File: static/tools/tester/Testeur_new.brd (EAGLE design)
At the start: 103.5 x 105.7 mm, 28 parts, among them IC1 MEGA8-P, SW1 CI-11

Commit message: [tester] add VCC pin for UART
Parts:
- removed UART: (no value), con-lstb:MA03-1
- added SV1: (no value), con-lstb:MA04-1
- moved R1 6.38 mm to (15.9, 9.53)
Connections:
- net GND: now also SV1.3; no longer UART.3
- net N$21: now also SV1.1; no longer UART.1
- net N$22: now also SV1.2; no longer UART.2
- net VCC: now also SV1.4
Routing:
- net N$4: track 5.39 -> 11.5 mm
- net VCC: track 162.1 -> 163.9 mm
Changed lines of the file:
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@@
 <?xml version="1.0" encoding="utf-8"?>
 <!DOCTYPE eagle SYSTEM "eagle.dtd">
-<eagle version="6.1">
+<eagle version="6.3">
 <drawing>
 <settings>
@@
 </class>
 </classes>
-<designrules>
+<designrules name="default">
 <description language="de">&lt;b&gt;EAGLE Design Rules&lt;/b&gt;
 &lt;p&gt;
@@
 <element name="C1-REGULATOR" library="capacitor-wima" package="C5B5" value="" x="31.75" y="41.275" rot="R270"/>
 <element name="C2-REGULATOR" library="capacitor-wima" package="C5B5" value="" x="46.99" y="41.275" rot="R270"/>
-<element name="R1" library="rcl" package="0204/5" value="" x="15.24" y="15.875" rot="R90"/>
+<element name="R1" library="rcl" package="0204/5" value="" x="15.875" y="9.525" rot="R90"/>
 <element name="RETURN" library="con-lstb" package="MA03-1" value="" x="10.16" y="31.115" rot="R180">
 <attribute name="OC_NEWARK" value="unknown" x="-33.02" y="81.915" size="1.778" layer="27" rot="R180" display="off"/>
@@
 <attribute name="MF" value="" x="-11.43" y="-47.625" size="1.778" layer="27" rot="R270" display="off"/>
 <attribute name="OC_FARNELL" value="unknown" x="-11.43" y="-47.625" size="1.778" layer="27" rot="R270" display="off"/>
-</element>
-<element name="UART" library="con-lstb" package="MA03-1" value="" x="19.05" y="12.065" rot="R270">
-<attribute name="OC_NEWARK" value="unknown" x="-38.1" y="-5.715" size="1.778" layer="27" rot="R270" display="off"/>
-<attribute name="MPN" value="" x="-38.1" y="-5.715" size="1.778" layer="27" rot="R270" display="off"/>
-<attribute name="MF" value="" x="-38.1" y="-5.715" size="1.778" layer="27" rot="R270" display="off"/>
-<attribute name="OC_FARNELL" value="unknown" x="-38.1" y="-5.715" size="1.778" layer="27" rot="R270" display="off"/>
 </element>
 <element name="I²C" library="con-lstb" package="MA04-1" value="" x="8.89" y="23.495">
@@
 <attribute name="MF" value="" x="93.98" y="12.7" size="1.778" layer="27" display="off"/>
 <attribute name="OC_FARNELL" value="unknown" x="93.98" y="12.7" size="1.778" layer="27" display="off"/>
+</element>
+<element name="SV1" library="con-lstb" package="MA04-1" value="" x="19.05" y="10.795" rot="R270">
+<attribute name="OC_NEWARK" value="unknown" x="19.05" y="10.795" size="1.778" layer="27" rot="R270" display="off"/>
+<attribute name="MPN" value="" x="19.05" y="10.795" size="1.778" layer="27" rot="R270" display="off"/>
+<attribute name="MF" value="" x="19.05" y="10.795" size="1.778" layer="27" rot="R270" display="off"/>
+<attribute name="OC_FARNELL" value="unknown" x="19.05" y="10.795" size="1.778" layer="27" rot="R270" display="off"/>
 </element>
 </elements>
@@
 <contactref element="IC1" pad="1"/>
 <contactref element="R1" pad="2"/>
-<wire x1="15.24" y1="18.415" x2="19.05" y2="22.225" width="0.8128" layer="16"/>
+<wire x1="15.875" y1="12.065" x2="15.875" y2="19.05" width="0.8128" layer="16"/>
+<wire x1="15.875" y1="19.05" x2="19.05" y2="22.225" width="0.8128" layer="16"/>
 </signal>
 <signal name="N$7">
@@
 <wire x1="41.91" y1="36.83" x2="39.37" y2="34.29" width="0.8128" layer="16"/>
 <wire x1="39.37" y1="34.29" x2="39.37" y2="29.845" width="0.8128" layer="16"/>
-<wire x1="15.24" y1="13.335" x2="10.16" y2="13.335" width="0.8128" layer="16"/>
 <wire x1="10.16" y1="13.335" x2="8.89" y2="14.605" width="0.8128" layer="16"/>
 <wire x1="8.89" y1="14.605" x2="8.89" y2="15.875" width="0.8128" layer="16"/>
@@
 <via x="34.29" y="19.05" extent="1-16" drill="0.8"/>
 <via x="31.75" y="7.62" extent="1-16" drill="0.8"/>
-<wire x1="26.67" y1="9.525" x2="24.13" y2="9.525" width="0.8128" layer="16"/>
-<wire x1="24.13" y1="9.525" x2="22.86" y2="10.795" width="0.8128" layer="16"/>
 <wire x1="29.845" y1="7.62" x2="27.94" y2="9.525" width="0.8128" layer="16"/>
 <wire x1="27.94" y1="9.525" x2="26.67" y2="9.525" width="0.8128" layer="16"/>
-<wire x1="15.24" y1="13.335" x2="15.24" y2="11.43" width="0.8128" layer="16"/>
-<wire x1="15.24" y1="11.43" x2="15.24" y2="9.525" width="0.8128" layer="1"/>
-<wire x1="15.24" y1="9.525" x2="17.145" y2="7.62" width="0.8128" layer="1"/>
-<wire x1="17.145" y1="7.62" x2="20.955" y2="7.62" width="0.8128" layer="1"/>
-<wire x1="20.955" y1="7.62" x2="22.86" y2="9.525" width="0.8128" layer="1"/>
-<wire x1="22.86" y1="9.525" x2="22.86" y2="10.795" width="0.8128" layer="1"/>
-<via x="15.24" y="11.43" extent="1-16" drill="0.8"/>
+<wire x1="15.875" y1="6.985" x2="15.875" y2="4.445" width="0.8128" layer="16"/>
+<wire x1="15.875" y1="4.445" x2="20.955" y2="4.445" width="0.8128" layer="1"/>
+<wire x1="20.955" y1="4.445" x2="22.86" y2="6.35" width="0.8128" layer="1"/>
+<wire x1="22.86" y1="6.35" x2="22.86" y2="10.795" width="0.8128" layer="1"/>
+<via x="15.875" y="4.445" extent="1-16" drill="0.8"/>
 <via x="22.86" y="10.795" extent="1-16" drill="0.8"/>
 <wire x1="12.7" y1="6.985" x2="7.62" y2="6.985" width="0.8128" layer="16"/>
@@
 <wire x1="3.81" y1="17.78" x2="5.08" y2="19.05" width="0.8128" layer="16"/>
 <wire x1="5.08" y1="19.05" x2="5.08" y2="20.32" width="0.8128" layer="16"/>
+<contactref element="SV1" pad="4"/>
+<wire x1="12.7" y1="6.985" x2="15.875" y2="6.985" width="0.8128" layer="16"/>
+<wire x1="19.05" y1="6.985" x2="15.875" y2="6.985" width="0.8128" layer="16"/>
+<wire x1="24.13" y1="9.525" x2="22.86" y2="10.795" width="0.8128" layer="16"/>
+<wire x1="26.67" y1="9.525" x2="24.13" y2="9.525" width="0.8128" layer="16"/>
 </signal>
 <signal name="GND">
@@
 <contactref element="POTAR-CONTRASTE" pad="3"/>
 <contactref element="CODER-MOTOR" pad="4"/>
-<contactref element="UART" pad="3"/>
 <contactref element="I²C" pad="2"/>
 <contactref element="IC1" pad="22"/>
@@
 <wire x1="7.62" y1="41.91" x2="7.62" y2="36.83" width="0.8128" layer="16"/>
 <wire x1="7.62" y1="36.83" x2="7.62" y2="31.115" width="0.8128" layer="16"/>
-<wire x1="19.05" y1="9.525" x2="19.685" y2="9.525" width="0.8128" layer="16"/>
-<wire x1="19.685" y1="9.525" x2="22.225" y2="6.985" width="0.8128" layer="16"/>
 <wire x1="22.225" y1="6.985" x2="26.67" y2="6.985" width="0.8128" layer="16"/>
 <wire x1="26.67" y1="6.985" x2="27.305" y2="6.985" width="0.8128" layer="16"/>
@@
 <wire x1="12.065" y1="43.815" x2="9.525" y2="43.815" width="0.8128" layer="16"/>
 <wire x1="9.525" y1="43.815" x2="7.62" y2="41.91" width="0.8128" layer="16"/>
-<wire x1="19.05" y1="9.525" x2="12.7" y2="9.525" width="0.8128" layer="16"/>
 <wire x1="12.7" y1="9.525" x2="7.62" y2="9.525" width="0.8128" layer="16"/>
 <wire x1="6.35" y1="15.875" x2="6.35" y2="13.97" width="0.8128" layer="16"/>
@@
 <wire x1="19.05" y1="41.275" x2="19.05" y2="42.545" width="0.8128" layer="16"/>
 <wire x1="34.29" y1="36.195" x2="31.75" y2="38.735" width="0.8128" layer="16"/>
+<contactref element="SV1" pad="3"/>
+<wire x1="12.7" y1="9.525" x2="19.05" y2="9.525" width="0.8128" layer="16"/>
+<wire x1="22.225" y1="6.985" x2="19.685" y2="9.525" width="0.8128" layer="16"/>
+<wire x1="19.685" y1="9.525" x2="19.05" y2="9.525" width="0.8128" layer="16"/>
 </signal>
 <signal name="N$14">
@@
 <signal name="N$21">
 <contactref element="IC1" pad="2"/>
-<contactref element="UART" pad="1"/>
-<wire x1="19.05" y1="14.605" x2="21.59" y2="17.145" width="0.8128" layer="16"/>
-<wire x1="21.59" y1="17.145" x2="21.59" y2="22.225" width="0.8128" layer="16"/>
+<wire x1="21.59" y1="16.51" x2="21.59" y2="22.225" width="0.8128" layer="16"/>
+<contactref element="SV1" pad="1"/>
+<wire x1="21.59" y1="16.51" x2="19.685" y2="14.605" width="0.8128" layer="16"/>
+<wire x1="19.685" y1="14.605" x2="19.05" y2="14.605" width="0.8128" layer="16"/>
 </signal>
 <signal name="N$22">
-<contactref element="UART" pad="2"/>
 <contactref element="IC1" pad="3"/>
 <wire x1="24.13" y1="22.225" x2="24.13" y2="15.875" width="0.8128" layer="16"/>
-<wire x1="24.13" y1="15.875" x2="20.32" y2="12.065" width="0.8128" layer="16"/>
-<wire x1="20.32" y1="12.065" x2="19.05" y2="12.065" width="0.8128" layer="16"/>
+<contactref element="SV1" pad="2"/>
+<wire x1="19.05" y1="12.065" x2="20.32" y2="12.065" width="0.8128" layer="16"/>
+<wire x1="20.32" y1="12.065" x2="24.13" y2="15.875" width="0.8128" layer="16"/>
 </signal>
 <signal name="N$25">

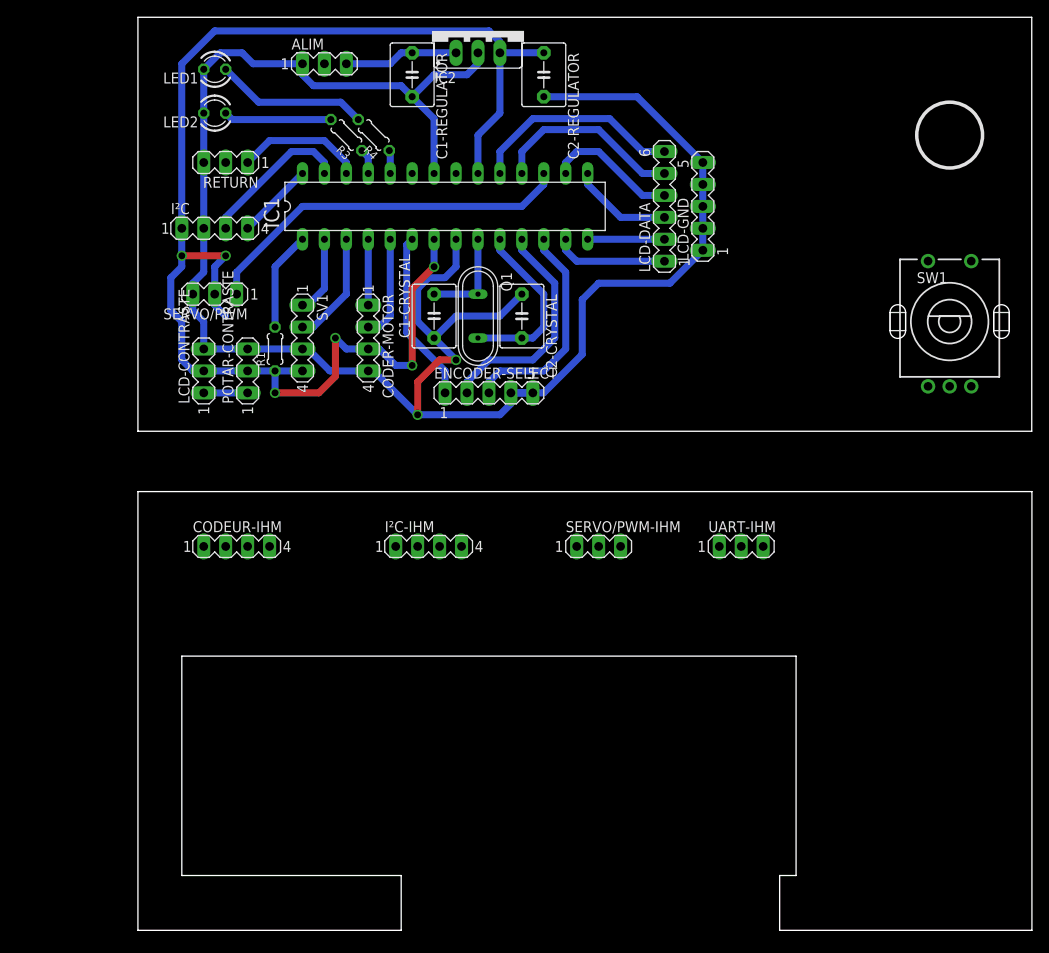
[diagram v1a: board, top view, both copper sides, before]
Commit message: [tester] create ihm board
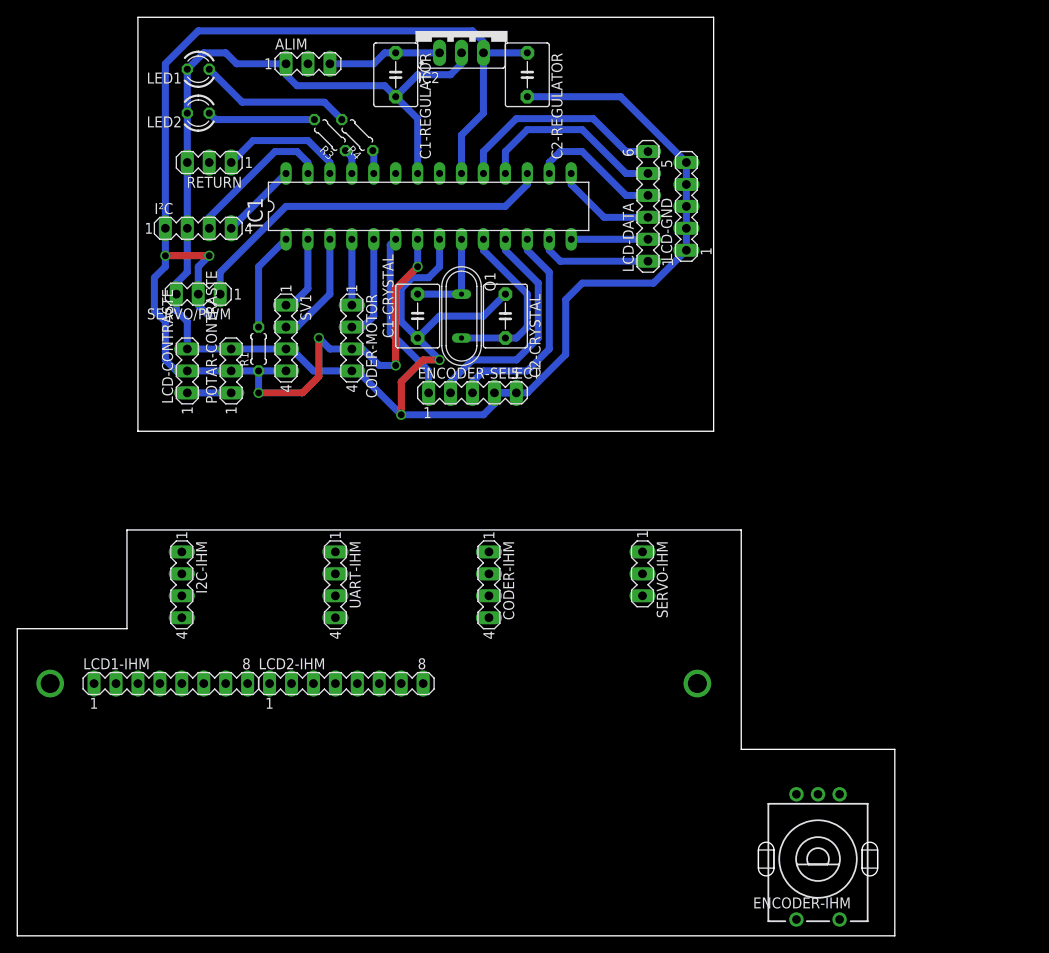
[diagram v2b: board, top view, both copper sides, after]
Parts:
- removed CODEUR-IHM, I²C-IHM: (no value), con-lstb:MA04-1
- removed SERVO/PWM-IHM: (no value), con-lstb:MA03-1
- removed SW1: CI-11, piher:CI-11
- added CODER-IHM, I2C-IHM: (no value), con-lstb:MA04-1
- added ENCODER-IHM: CI-11, piher:CI-11
- added LCD1-IHM, LCD2-IHM: (no value), con-lstb:MA08-1
- added SERVO-IHM: (no value), con-lstb:MA03-1
- UART-IHM: device con-lstb:MA03-1 -> con-lstb:MA04-1
- moved UART-IHM 47.2 mm to (22.9, -17.8), turned to 270 degrees
- moved ALIM 1.91 mm to (19.7, 42.5)
- moved C1-CRYSTAL 1.91 mm to (32.4, 13.3)
- moved C1-REGULATOR 1.91 mm to (29.8, 41.3)
- moved C2-CRYSTAL 1.91 mm to (42.5, 13.3)
- moved C2-REGULATOR 1.91 mm to (45.1, 41.3)
- moved CODER-MOTOR 1.91 mm to (24.8, 10.8)
- moved ENCODER-SELECT 1.91 mm to (38.7, 4.45)
- moved IC1 1.91 mm to (33.7, 26.0)
- moved LCD-DATA 1.91 mm to (59.1, 26.0)
- moved LCD-GND 1.91 mm to (63.5, 26.0)
- moved R4 1.91 mm to (25.4, 34.3)
- moved SV1 1.91 mm to (17.1, 10.8)
- moved I²C 1.91 mm to (6.99, 23.5)
- moved LCD-CONTRASTE 1.91 mm to (5.71, 6.99)
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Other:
- board size 103.5 x 105.7 mm -> 101.6 x 106.3 mm

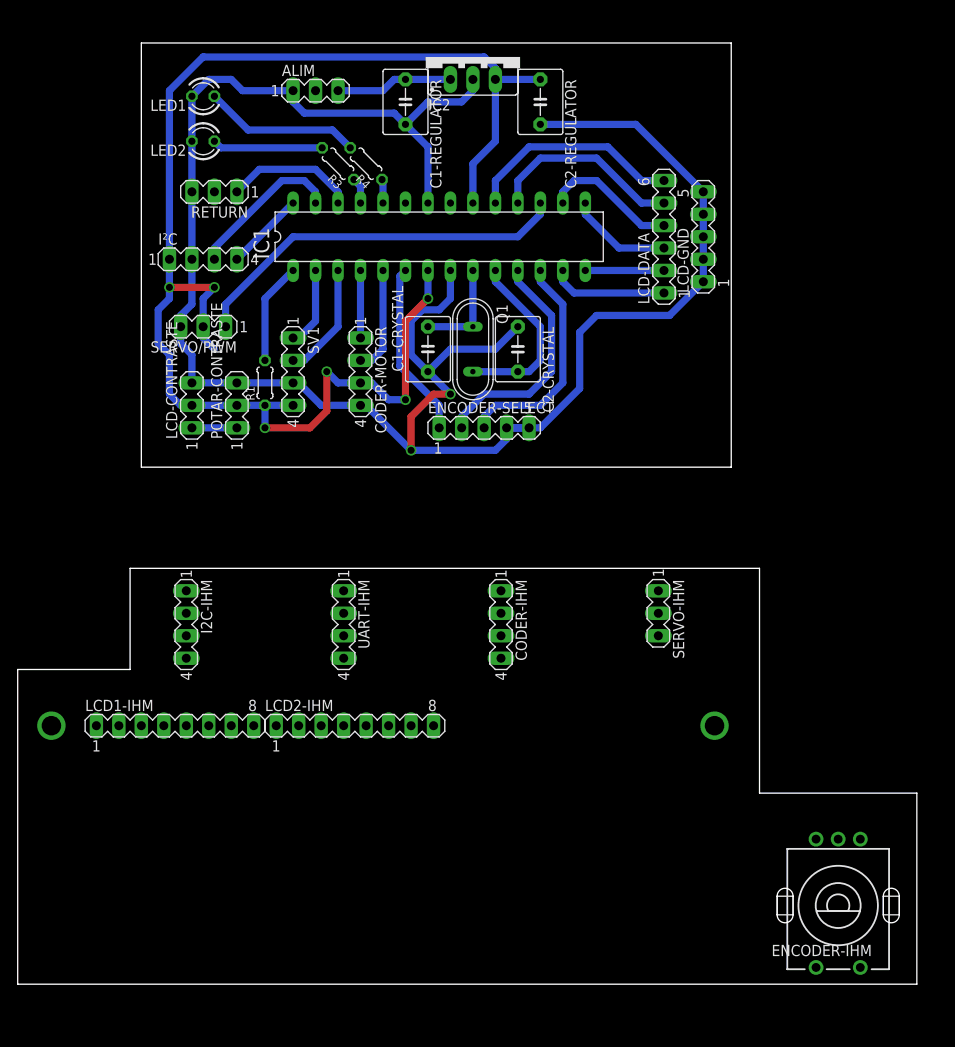
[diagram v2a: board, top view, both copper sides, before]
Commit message: [tester]move holes to make a good design
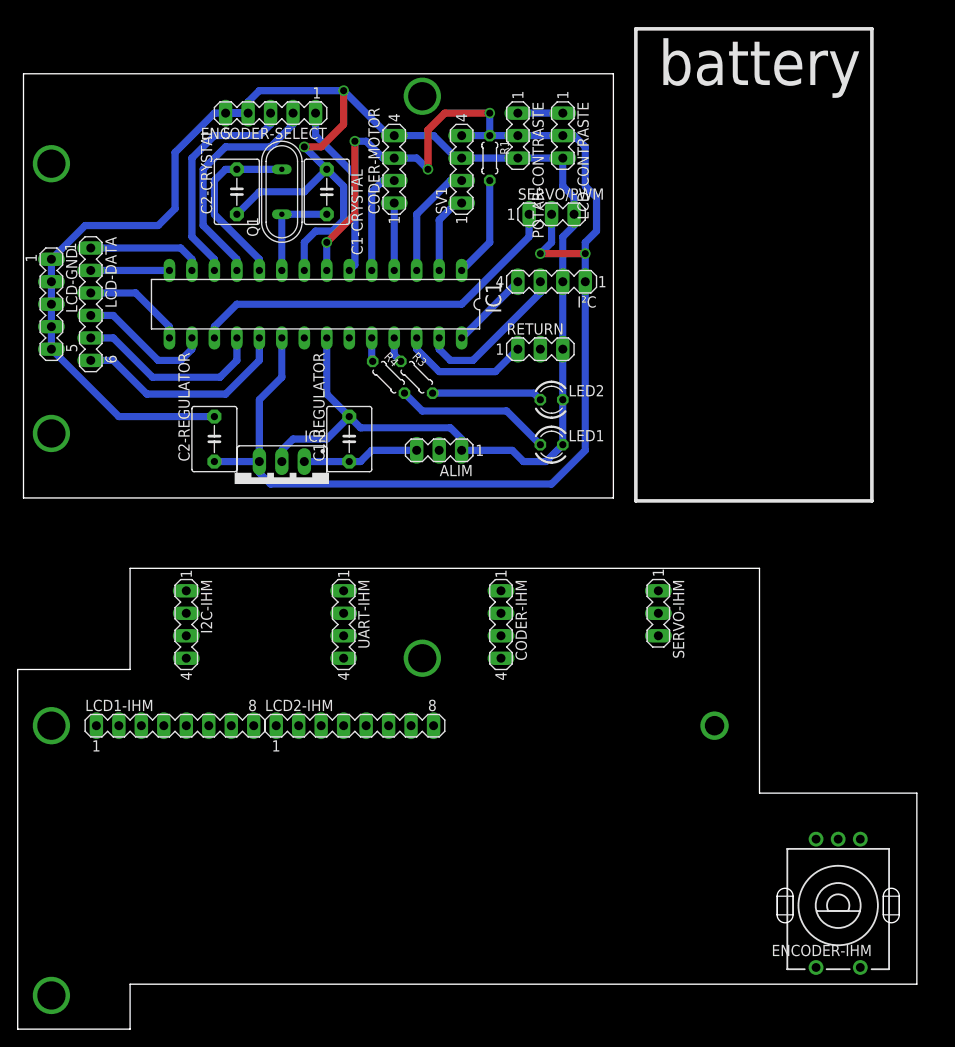
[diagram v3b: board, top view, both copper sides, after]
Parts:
- moved LCD-GND 74.1 mm to (-10.2, 18.4), turned to 270 degrees
- moved LCD-DATA 65.2 mm to (-5.71, 18.4), turned to 270 degrees
- moved LED1 55.7 mm to (46.4, 2.54), turned to 0 degrees
- moved C2-REGULATOR 53.0 mm to (8.26, 3.17), turned to 90 degrees
- moved IC2 52.9 mm to (15.9, -1.91), turned to 180 degrees
- moved LCD-CONTRASTE 51.8 mm to (47.6, 37.5), turned to 270 degrees
- moved LED2 49.0 mm to (46.4, 7.62), turned to 0 degrees
- moved POTAR-CONTRASTE 44.0 mm to (42.5, 37.5), turned to 270 degrees
- moved ALIM 43.0 mm to (33.7, 1.91), turned to 180 degrees
- moved ENCODER-SELECT 43.0 mm to (14.6, 40.0), turned to 180 degrees
- moved SERVO/PWM 41.4 mm to (46.4, 28.6), turned to 0 degrees
- moved RETURN 40.9 mm to (45.1, 13.3), turned to 0 degrees
- moved I²C 39.5 mm to (46.4, 21.0), turned to 180 degrees
- moved C1-REGULATOR 38.6 mm to (23.5, 3.17), turned to 90 degrees
- moved C2-CRYSTAL 36.4 mm to (10.8, 31.1), turned to 90 degrees
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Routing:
- net VCC: track 163.9 -> 160.4 mm
- net N$16: track 22.2 -> 21.7 mm
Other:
- board size 101.6 x 106.3 mm -> 101.6 x 108 mm
- board text added: "battery"
